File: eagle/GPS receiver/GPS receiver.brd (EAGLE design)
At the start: 25 x 25 mm, 5 parts, among them U2 ORG1411

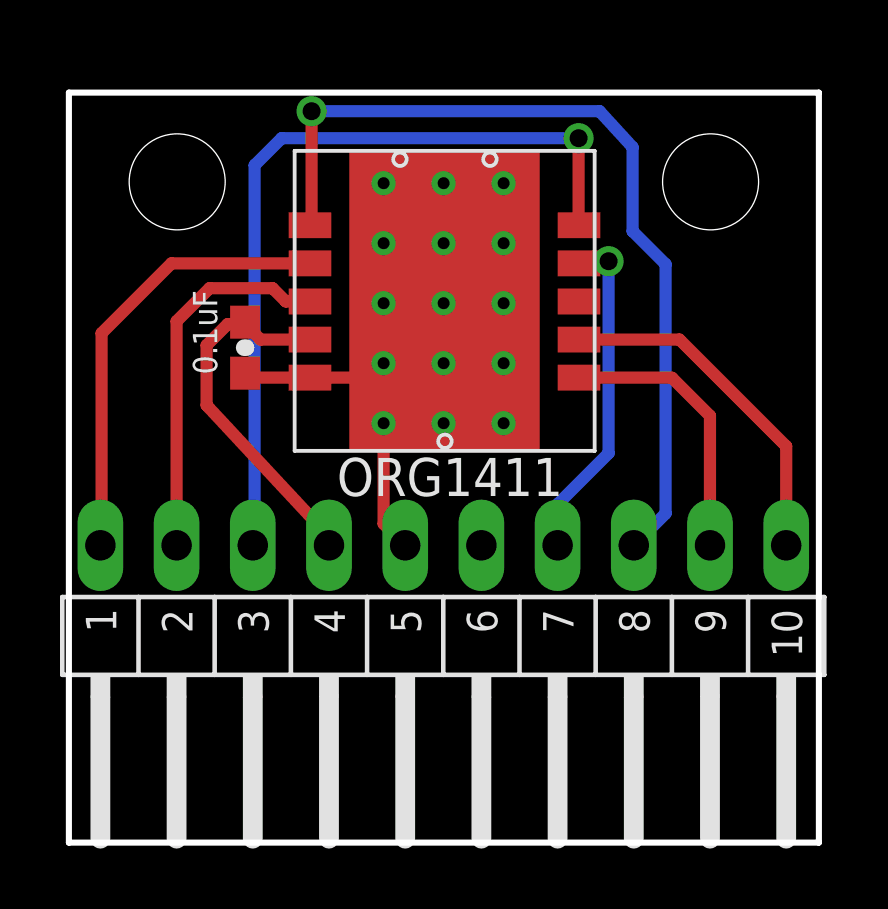
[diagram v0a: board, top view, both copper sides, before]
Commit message: Design update
Add backup battery
Add jumper to select between i2c or UART default interface
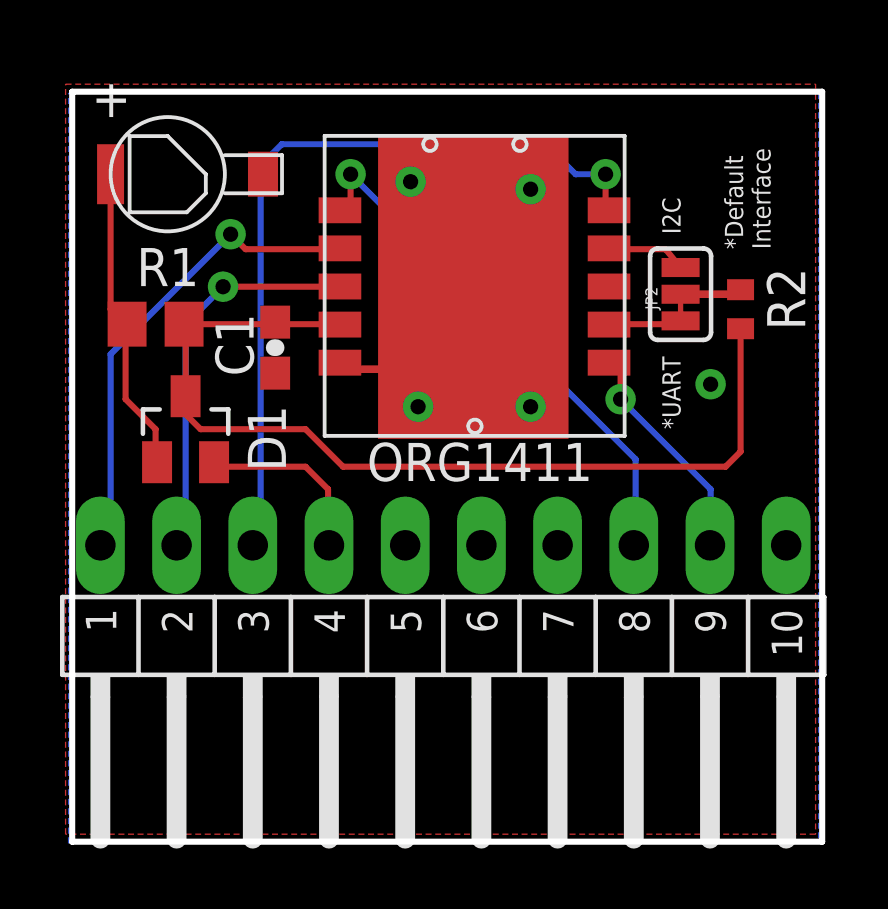
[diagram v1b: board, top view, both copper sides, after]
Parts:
- removed U$1: (no value), theairboard:LAYOUT25X25
- added C2: 0.03F, hidnSeek:PAS311-VA6R
- added D1: (no value), diode:SOT23
- added JP2: JUMPER-3SMD, SparkFun-Retired:SJ_3
- added R1: 56, rcl:R0805
- added R2: 1K, rcl:R0402
- added U$2: (no value), theairboard:LAYOUT25X25WO
- moved U2 1.12 mm to (18.1, 35.3)
- moved C1 1.00 mm to (16.0, 30.7)
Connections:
- removed net CTS: JP1.10, U2.7
- removed net RTS: JP1.7, U2.9
- new net I2C: JP2.3, U2.9
- new net N$3: C1.1, D1.3, R1.2, R2.2, U2.4
- new net N$4: C2.+, D1.1, R1.1
- new net SER: JP2.1, JP2.2, R2.1, U2.7
- net GND: now also C2.-, U2.GND
- net VCC: now also D1.2; no longer C1.1, U2.4
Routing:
- net N$3: track 0.00 -> 32.3 mm
- net GND: track 37.2 -> 5.94 mm, vias 15 -> 5
- net CTS: track 11.7 -> 0.00 mm
- net RTS: track 11.2 -> 0.00 mm, vias 1 -> 0
- net ONOFF: track 29.3 -> 18.3 mm
- net N$4: track 0.00 -> 11.0 mm
- net VCC: track 12.3 -> 6.09 mm
- net SER: track 0.00 -> 5.45 mm
- net I2C: track 0.00 -> 2.91 mm
- net WUP: track 9.21 -> 7.56 mm, vias 0 -> 1
- net 1PPS: track 15.0 -> 16.0 mm, vias 0 -> 1
- net TX: track 12.6 -> 13.1 mm, vias 0 -> 1
- added copper zone on layer 1, net GND
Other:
- board text added: "*Default Interface"
- board text added: "*UART"
- board text added: "I2C"

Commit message: Update
Add resistor on /RESET input to automatic shutdown the receiver when no
primary supply
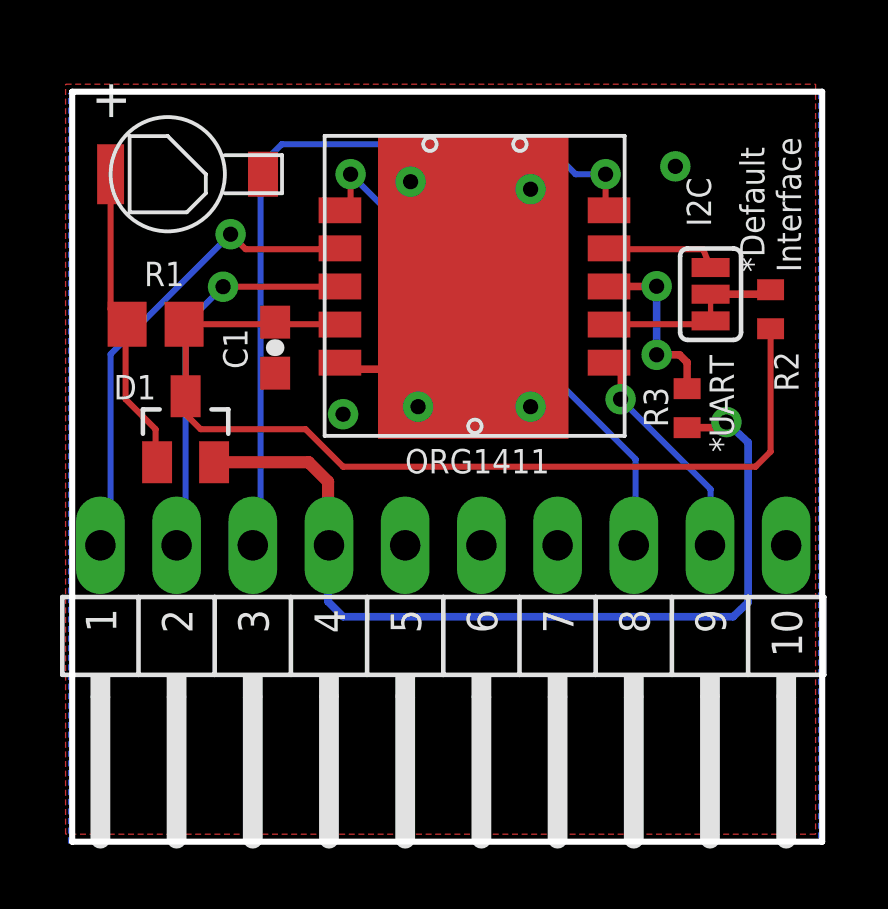
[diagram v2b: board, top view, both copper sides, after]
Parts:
- added R3: 1K, rcl:R0402
- D1: value (none) -> SB05W05C
- moved JP2 1.00 mm to (30.5, 32.5)
- moved R2 1.00 mm to (32.5, 32.0)
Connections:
- new net +3V3: D1.2, JP1.4, R3.1
- net N$3: now also R3.2, U2.8; no longer C1.1, D1.3, R1.2, R2.2, U2.4
- net VCC: now also C1.1, D1.3, R1.2, R2.2, U2.4; no longer D1.2, JP1.4
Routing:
- net +3V3: track 0.00 -> 30.2 mm, vias 0 -> 1
- net VCC: track 6.09 -> 33.3 mm
- net N$3: track 32.3 -> 5.87 mm, vias 0 -> 2
- net I2C: track 2.91 -> 4.03 mm
- net SER: track 5.45 -> 6.15 mm
- net GND: vias 5 -> 6
